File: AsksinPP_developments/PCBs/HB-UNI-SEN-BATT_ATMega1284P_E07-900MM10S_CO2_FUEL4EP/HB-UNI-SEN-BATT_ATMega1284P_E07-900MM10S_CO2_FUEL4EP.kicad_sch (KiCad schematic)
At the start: 82 parts, among them J1 Conn_01x02, J10 charge, J11 ePaper connector, J12 FTDI Debuger, J13 U.FL connector, J2 Conn_01x02, J3 Conn_01x02, J4 Conn_01x02, J5 ISP Programmer, Q1 IRLU024N, Q2 FDN304P, Q3 FDN304P, Q4 FDN304P, SW1 Config button, SW2 Reset button, U1 ATmega1284P-AU, U2 TPS61221DCK, U3 BME280, Y1 8MHz

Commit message: PCB updates
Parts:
- D1: value LED red 3mm -> LED red SMD
- D2, D3, D4: LCSC C84256 -> (none); TYPE LED_0805 -> (none)
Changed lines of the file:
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@@
 	(title_block
 		(title "HB-UNI-SEN-BATT_ATMega1284P_E07-900MM10S_CO2_FUEL4EP")
-		(date "2025-06-26")
-		(rev "1.0")
+		(date "2026-03-09")
+		(rev "1.1")
 		(company "FUEL4EP")
 		(comment 1 "Creative Commons License, non-commercial")
@@
 			)
 		)
-		(property "Value" "LED red 3mm"
+		(property "Value" "LED red SMD"
 			(at 114.3 158.75 0)
 			(effects
@@
 			)
 		)
-		(property "TYPE" "LED_0805"
+		(property "TYPE" ""
 			(at 34.29 186.69 0)
 			(effects
@@
 			)
 		)
-		(property "LCSC" "C84256"
+		(property "LCSC" ""
 			(at 34.29 186.69 0)
 			(effects
@@
 			)
 		)
-		(property "TYPE" "LED_0805"
+		(property "TYPE" ""
 			(at 34.29 168.91 0)
 			(effects
@@
 			)
 		)
-		(property "LCSC" "C84256"
+		(property "LCSC" ""
 			(at 34.29 168.91 0)
 			(effects
@@
 			)
 		)
-		(property "TYPE" "LED_0805"
+		(property "TYPE" ""
 			(at 34.29 177.8 0)
 			(effects
@@
 			)
 		)
-		(property "LCSC" "C84256"
+		(property "LCSC" ""
 			(at 34.29 177.8 0)
 			(effects

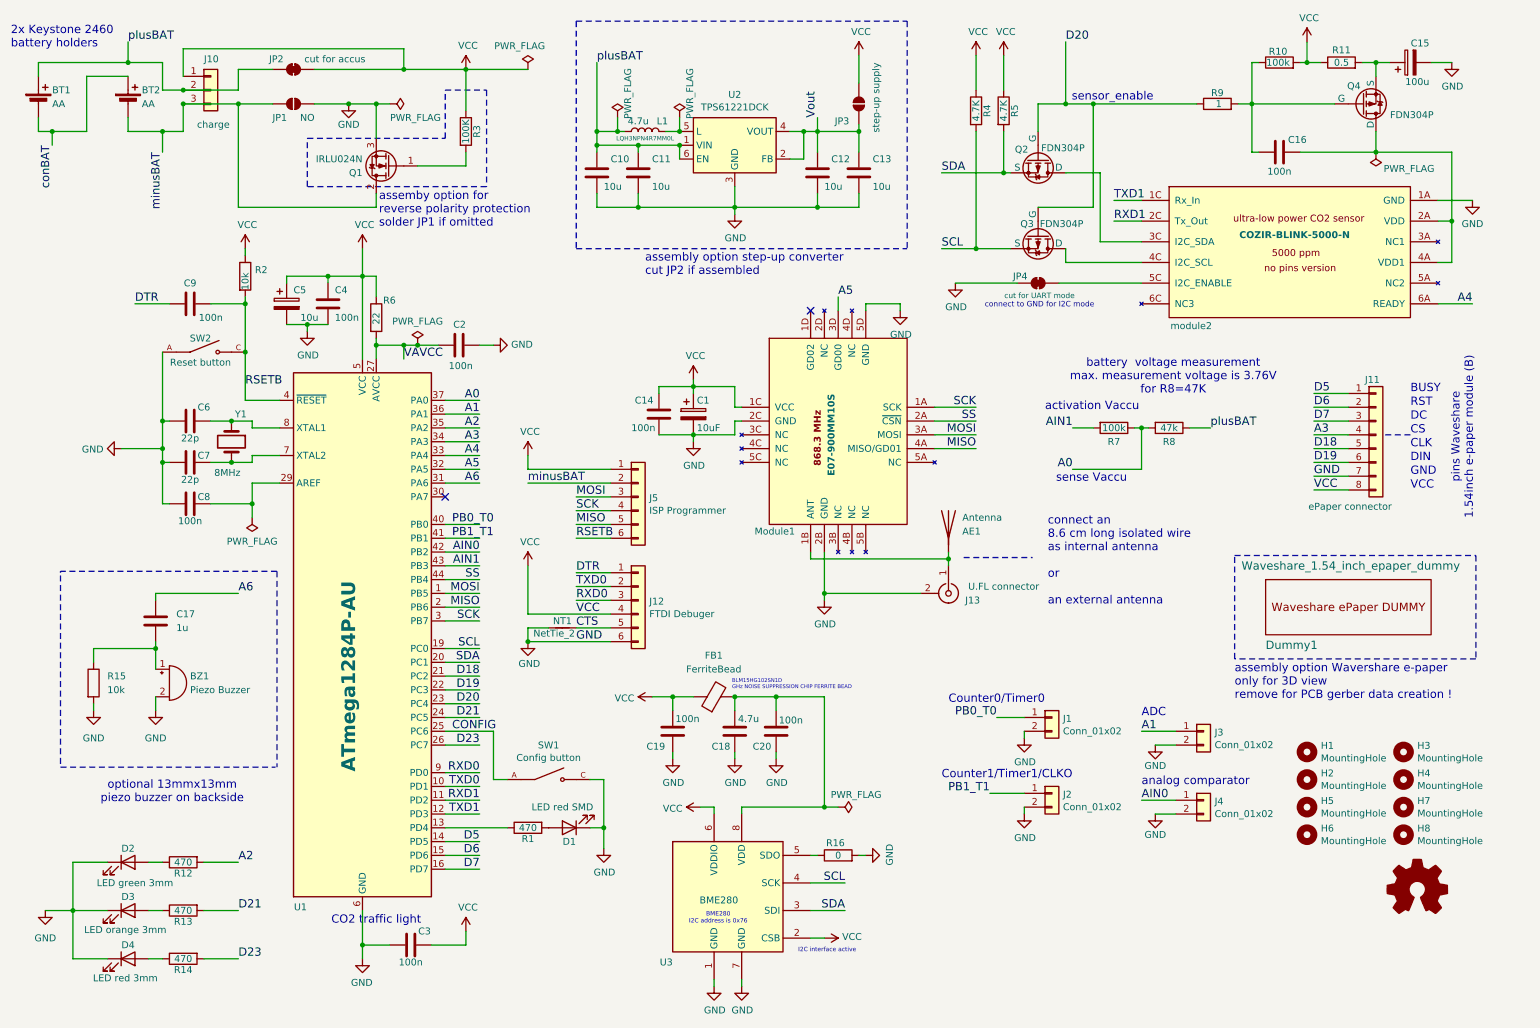
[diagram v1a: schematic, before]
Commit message: HB-UNI-SEN-BATT_ATMega1284P_E07-900MM10S_CO2_FUEL4EP: added warning in README.md not to uuse because of fatal  errors of PCB
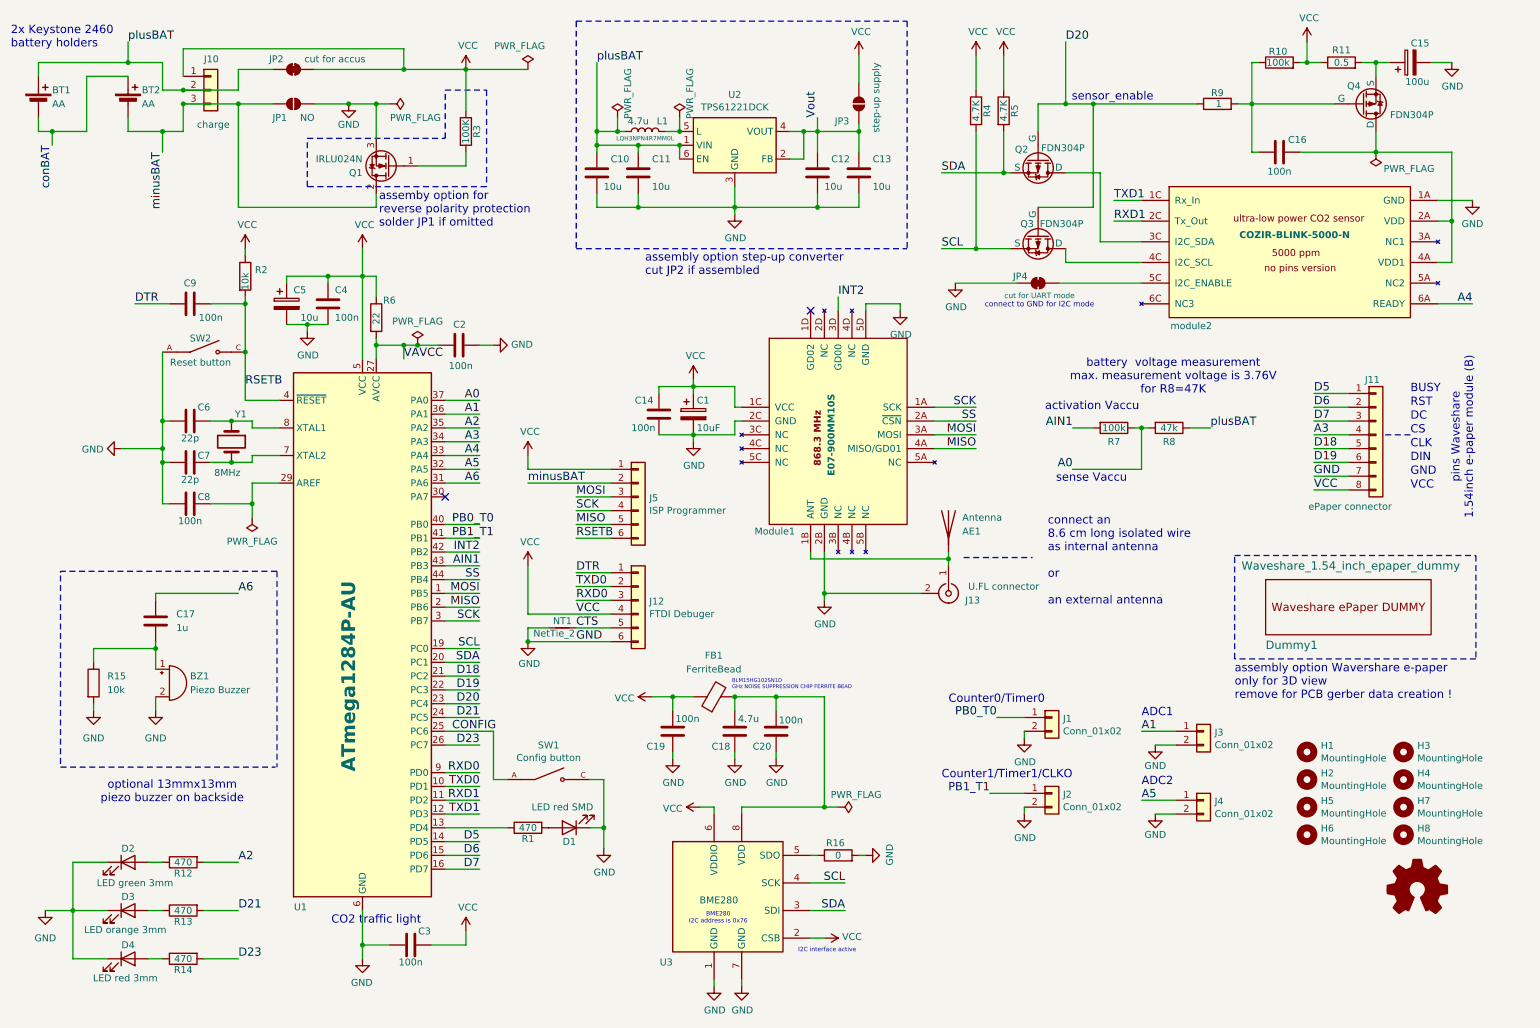
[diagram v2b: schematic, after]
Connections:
- net A5: now also J4.1 (Pin_1); no longer Module1.3D (GD00)
- net AIN0 renamed INT2
- net INT2: now also Module1.3D (GD00); no longer J4.1 (Pin_1)
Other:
- note added: "ADC1"
- note added: "ADC2"
- note removed: "ADC"
- note removed: "analog comparator"
